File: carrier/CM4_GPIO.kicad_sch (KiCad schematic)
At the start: 19 parts, among them J19 Left GPIO, J20 Right GPIO, J5 System, SW1 BT/WL Dis, U10 MagJack-A70-112-331N126, U6 74LVC1G07SE-7, U7 TPD4EUSB30, U8 TPD4EUSB30, U9 74LVC1G07SE-7

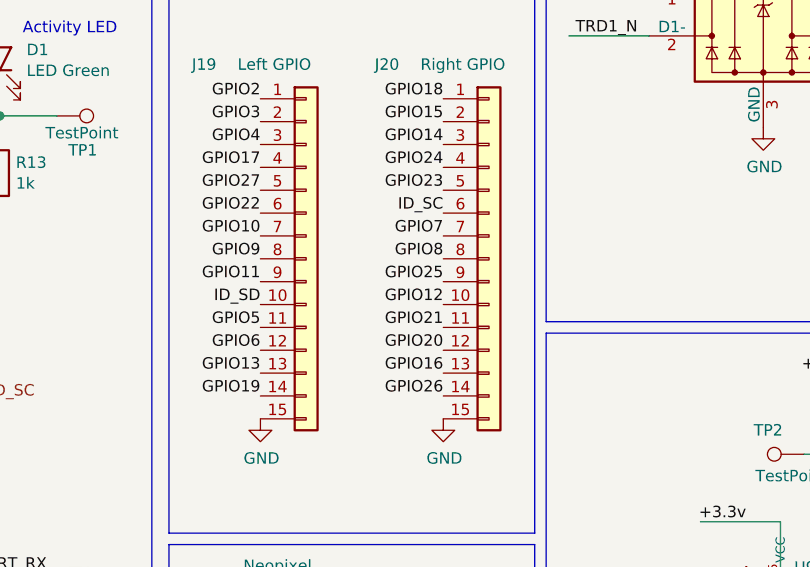
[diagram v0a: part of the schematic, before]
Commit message: Feat: routed non-important traces on carrier board
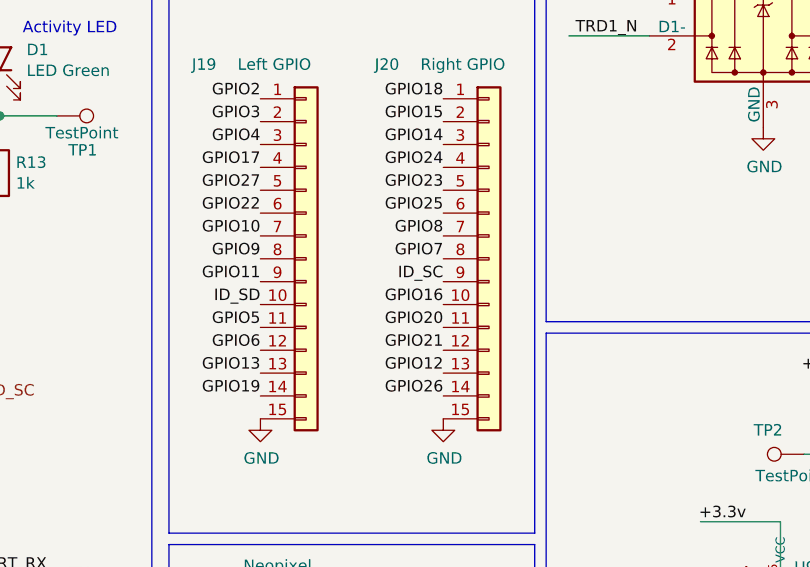
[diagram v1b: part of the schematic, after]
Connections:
- net GPIO12: now also J20.13 (Pin_13); no longer J20.10 (Pin_10)
- net GPIO16: now also J20.10 (Pin_10); no longer J20.13 (Pin_13)
- net GPIO20: now also J20.11 (Pin_11); no longer J20.12 (Pin_12)
- net GPIO21: now also J20.12 (Pin_12); no longer J20.11 (Pin_11)
- net GPIO25: now also J20.6 (Pin_6); no longer J20.9 (Pin_9)
- net GPIO7: now also J20.8 (Pin_8); no longer J20.7 (Pin_7)
- net GPIO8: now also J20.7 (Pin_7); no longer J20.8 (Pin_8)
- net ID_SC: now also J20.9 (Pin_9); no longer J20.6 (Pin_6)
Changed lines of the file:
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@@
     (effects (font (size 1.27 1.27)) (justify right bottom))
   )
-  (label "GPIO12" (at 163.83 93.98 180) (fields_autoplaced)
+  (label "GPIO12" (at 163.83 101.6 180) (fields_autoplaced)
     (effects (font (size 1.27 1.27)) (justify right bottom))
   )
@@
     (effects (font (size 1.27 1.27)) (justify right bottom))
   )
-  (label "GPIO8" (at 163.83 88.9 180) (fields_autoplaced)
+  (label "GPIO8" (at 163.83 86.36 180) (fields_autoplaced)
     (effects (font (size 1.27 1.27)) (justify right bottom))
   )
@@
     (effects (font (size 1.27 1.27)) (justify right bottom))
   )
-  (label "GPIO20" (at 163.83 99.06 180) (fields_autoplaced)
+  (label "GPIO20" (at 163.83 96.52 180) (fields_autoplaced)
     (effects (font (size 1.27 1.27)) (justify right bottom))
   )
@@
     (effects (font (size 1.27 1.27)) (justify right bottom))
   )
-  (label "ID_SC" (at 163.83 83.82 180) (fields_autoplaced)
+  (label "ID_SC" (at 163.83 91.44 180) (fields_autoplaced)
     (effects (font (size 1.27 1.27)) (justify right bottom))
   )
@@
     (effects (font (size 1.27 1.27)) (justify right bottom))
   )
-  (label "GPIO7" (at 163.83 86.36 180) (fields_autoplaced)
+  (label "GPIO7" (at 163.83 88.9 180) (fields_autoplaced)
     (effects (font (size 1.27 1.27)) (justify right bottom))
   )
@@
     (effects (font (size 1.27 1.27)) (justify right bottom))
   )
-  (label "GPIO25" (at 163.83 91.44 180) (fields_autoplaced)
+  (label "GPIO25" (at 163.83 83.82 180) (fields_autoplaced)
     (effects (font (size 1.27 1.27)) (justify right bottom))
   )
@@
     (effects (font (size 1.27 1.27)) (justify right bottom))
   )
-  (label "GPIO16" (at 163.83 101.6 180) (fields_autoplaced)
-    (effects (font (size 1.27 1.27)) (justify right bottom))
-  )
-  (label "GPIO21" (at 163.83 96.52 180) (fields_autoplaced)
-    (effects (font (size 1.27 1.27)) (justify right bottom))
-  )
+  (label "GPIO16" (at 163.83 93.98 180) (fields_autoplaced)
+    (effects (font (size 1.27 1.27)) (justify right bottom))
+  )
+  (label "GPIO21" (at 163.83 99.06 180) (fields_autoplaced)
+    (effects (font (size 1.27 1.27)) (justify right bottom))
+  )

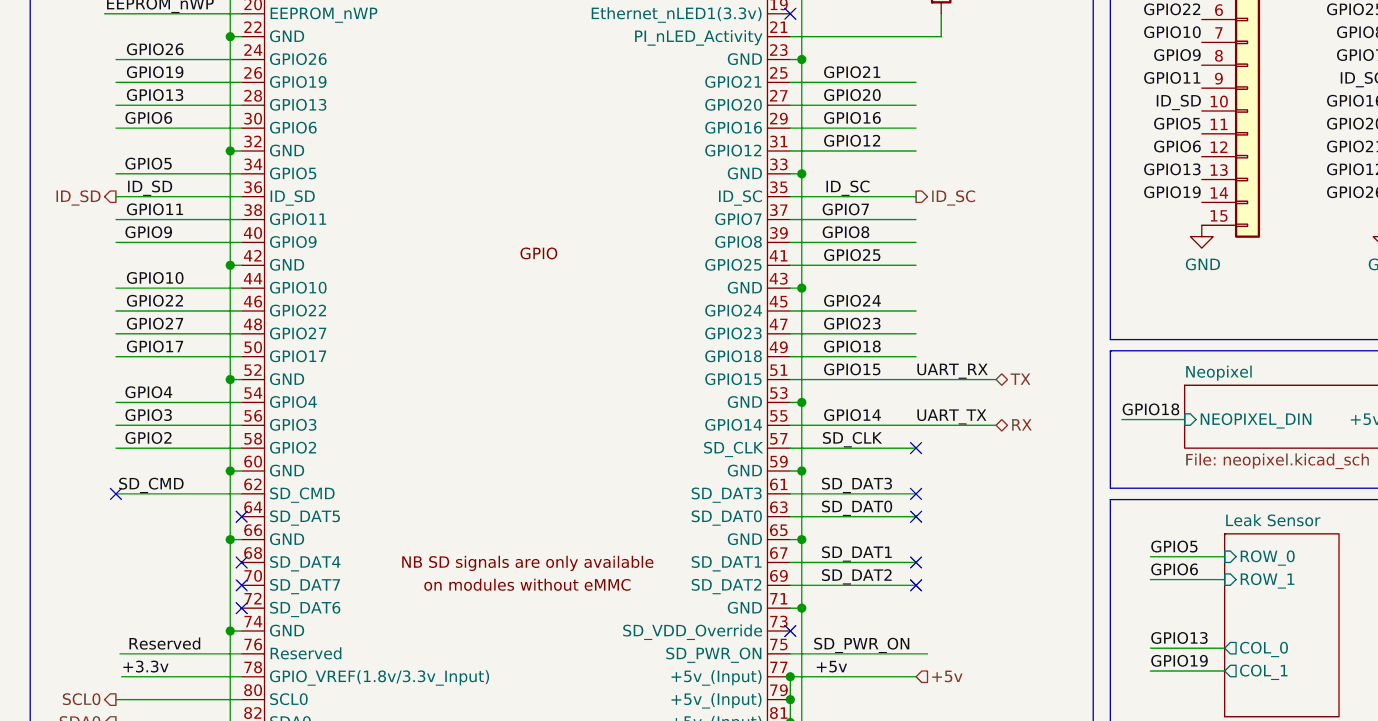
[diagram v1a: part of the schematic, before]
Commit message: Feat: conforms to jlc specs and (mostly) kicad DRC
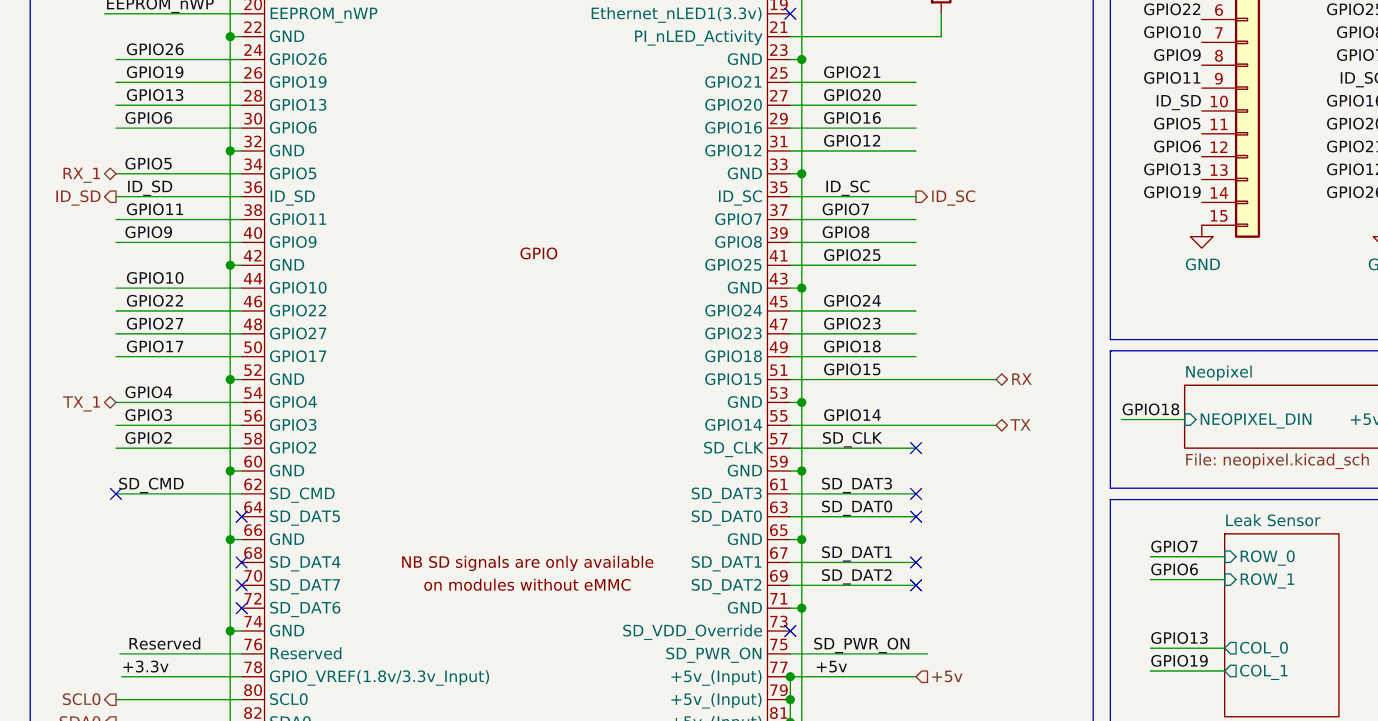
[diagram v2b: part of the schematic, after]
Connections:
- net RX: now also J20.2 (Pin_2), Module1.51 (GPIO15); no longer J20.3 (Pin_3), Module1.55 (GPIO14)
- net TX: now also J20.3 (Pin_3), Module1.55 (GPIO14); no longer J20.2 (Pin_2), Module1.51 (GPIO15)
- net GPIO4 renamed TX_1
- net GPIO5 renamed RX_1
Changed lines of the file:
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@@
     (effects (font (size 1.27 1.27)) (justify right bottom))
   )
-  (label "GPIO5" (at 137.795 143.51 0) (fields_autoplaced)
+  (label "GPIO7" (at 137.795 143.51 0) (fields_autoplaced)
     (effects (font (size 1.27 1.27)) (justify left bottom))
   )
@@
     (effects (font (size 1.27 1.27)) (justify right bottom))
   )
-  (label "UART_TX" (at 111.76 128.905 0) (fields_autoplaced)
-    (effects (font (size 1.27 1.27)) (justify left bottom))
-  )
   (label "GPIO15" (at 163.83 73.66 180) (fields_autoplaced)
     (effects (font (size 1.27 1.27)) (justify right bottom))
@@
     (effects (font (size 1.27 1.27)) (justify right bottom))
   )
-  (label "UART_RX" (at 111.76 123.825 0) (fields_autoplaced)
-    (effects (font (size 1.27 1.27)) (justify left bottom))
-  )
   (label "GPIO14" (at 163.83 76.2 180) (fields_autoplaced)
     (effects (font (size 1.27 1.27)) (justify right bottom))
@@
     (effects (font (size 1.27 1.27)) (justify right))
   )
-  (hierarchical_label "RX" (shape bidirectional) (at 120.65 128.905 0) (fields_autoplaced)
+  (hierarchical_label "RX" (shape bidirectional) (at 120.65 123.825 0) (fields_autoplaced)
     (effects (font (size 1.27 1.27)) (justify left))
   )
@@
     (effects (font (size 1.27 1.27)) (justify right))
   )
-  (hierarchical_label "TX" (shape bidirectional) (at 120.65 123.825 0) (fields_autoplaced)
+  (hierarchical_label "TX" (shape bidirectional) (at 120.65 128.905 0) (fields_autoplaced)
     (effects (font (size 1.27 1.27)) (justify left))
   )
@@
     (effects (font (size 1.27 1.27)) (justify left))
   )
+  (hierarchical_label "TX_1" (shape bidirectional) (at 22.86 126.365 180) (fields_autoplaced)
+    (effects (font (size 1.27 1.27)) (justify right))
+  )
+  (hierarchical_label "RX_1" (shape bidirectional) (at 22.86 100.965 180) (fields_autoplaced)
+    (effects (font (size 1.27 1.27)) (justify right))
+  )
   (hierarchical_label "SCL0" (shape output) (at 22.86 159.385 180) (fields_autoplaced)

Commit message: Feat: fixes all around, refactored project and working on CM4 POS file
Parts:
- SW1: value BT/WL Dis -> SW_DIP_x02
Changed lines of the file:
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@@
   (junction (at 97.79 167.005) (diameter 1.016) (color 0 0 0 0)
   )
-  (junction (at 161.29 182.88) (diameter 0) (color 0 0 0 0)
-  )
   (junction (at 97.79 159.385) (diameter 1.016) (color 0 0 0 0)
   )
@@
   )
   (junction (at 97.79 156.845) (diameter 1.016) (color 0 0 0 0)
+  )
+  (junction (at 161.29 180.34) (diameter 0) (color 0 0 0 0)
   )
   (junction (at 99.06 141.605) (diameter 1.016) (color 0 0 0 0)
@@
     (stroke (width 0) (type solid))
   )
+  (wire (pts (xy 161.29 180.34) (xy 161.29 182.88))
+    (stroke (width 0) (type default))
+  )
   (wire (pts (xy 22.86 118.745) (xy 36.83 118.745))
     (stroke (width 0) (type solid))
@@
     (stroke (width 0) (type solid))
   )
-  (wire (pts (xy 161.29 180.34) (xy 161.29 182.88))
+  (wire (pts (xy 161.29 177.8) (xy 161.29 180.34))
     (stroke (width 0) (type default))
   )
@@
     (effects (font (size 1.27 1.27)) (justify right bottom))
   )
-  (label "WL_nDis" (at 146.05 182.88 180) (fields_autoplaced)
+  (label "WL_nDis" (at 146.05 180.34 180) (fields_autoplaced)
     (effects (font (size 1.27 1.27)) (justify right bottom))
   )
@@
     (effects (font (size 1.27 1.27)) (justify right bottom))
   )
-  (label "BT_nDis" (at 146.05 180.34 180) (fields_autoplaced)
+  (label "BT_nDis" (at 146.05 177.8 180) (fields_autoplaced)
     (effects (font (size 1.27 1.27)) (justify right bottom))
   )
@@
         (path "/e63e39d7-6ac0-4ffd-8aa3-1841a4541b55/00000000-0000-0000-0000-00005cff706a"
           (reference "#PWR0110") (unit 1)
+        )
+      )
+    )
+  )
+  (symbol (lib_id "Switch:SW_DIP_x02") (at 153.67 180.34 0) (unit 1)
+    (in_bom yes) (on_board yes) (dnp no) (fields_autoplaced)
+    (property "Reference" "SW1" (at 153.67 171.45 0)
+      (effects (font (size 1.27 1.27)))
+    )
+    (property "Value" "SW_DIP_x02" (at 153.67 173.99 0)
+      (effects (font (size 1.27 1.27)))
+    )
+    (property "Footprint" "Button_Switch_SMD:SW_DIP_SPSTx02_Slide_Omron_A6H-2101_W6.15mm_P1.27mm" (at 153.67 180.34 0)
+      (effects (font (size 1.27 1.27)) hide)
+    )
+    (property "Datasheet" "~" (at 153.67 180.34 0)
+      (effects (font (size 1.27 1.27)) hide)
+    )
+    (pin "1")
+    (pin "2")
+    (pin "3")
+    (pin "4")
+    (instances
+      (project "carrier"
+        (path "/4b1cea9d-93bc-4380-88c3-ede99bb53de2/620225a5-f804-40cd-b5ea-f876279ff075"
+          (reference "SW1") (unit 1)
         )
       )
@@
         )
       )
-    )
-  )
-  (symbol (lib_id "Switch:SW_DIP_x02") (at 153.67 182.88 0) (unit 1)
-    (in_bom yes) (on_board yes) (dnp no) (fields_autoplaced)
-    (property "Reference" "SW1" (at 153.67 173.355 0)
-      (effects (font (size 1.27 1.27)))
-    )
-    (property "Value" "BT/WL Dis" (at 153.67 175.895 0)
-      (effects (font (size 1.27 1.27)))
-    )
-    (property "Footprint" "Button_Switch_SMD:SW_DIP_SPSTx02_Slide_Omron_A6H-2101_W6.15mm_P1.27mm" (at 153.67 182.88 0)
-      (effects (font (size 1.27 1.27)) hide)
-    )
-    (property "Datasheet" "~" (at 153.67 182.88 0)
-      (effects (font (size 1.27 1.27)) hide)
-    )
-    (pin "1")
-    (pin "2")
-    (pin "3")
-    (pin "4")
-    (instances
-      (project "carrier"
-        (path "/4b1cea9d-93bc-4380-88c3-ede99bb53de2/620225a5-f804-40cd-b5ea-f876279ff075"
-          (reference "SW1") (unit 1)
-        )
-      )
